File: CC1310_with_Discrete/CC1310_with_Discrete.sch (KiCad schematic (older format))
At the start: 75 parts, among them P1 CONN_02X03, P2 JTAG, P3 XBEE, SW1 RESET, SW2 USER_BUTTON, U1 TPS63051, U2 CC1310_7x7, U3 LTR-303ALS, U4 Si7006, U5 SMA_EDGE_CONNECTOR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

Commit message: added footprints the schematic
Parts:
- C1, C12, C14, C16, C17, C20, C25, C26, C28, C29, C33, C34, C8, C9, FL1: footprint (none) -> Capacitors_SMD:C_0603
- C10, C11, C13, C15, C18, C19, C2, C21, C22, C23, C24, C27, C30, C31, C32, C4, C5, C6, C7, L3, L4: footprint (none) -> Capacitors_SMD:C_0402
- C3: footprint Capacitors_SMD:C_0402 -> Capacitors_SMD:C_0603
- D1, D2, D3, D4: footprint (none) -> LEDs:LED_0805
- L1: footprint (none) -> Choke_SMD:Choke_SMD_1206_Handsoldering
- P1: footprint (none) -> Socket_Strips:Socket_Strip_Angled_2x03
- P2: footprint (none) -> Socket_Strips:Socket_Strip_Angled_2x05
- P3: footprint (none) -> Pin_Headers:Pin_Header_Straight_1x10_Pitch2.00mm
- R1, R2, R3, R4, R8, R9: footprint (none) -> Resistors_SMD:R_0402
- R10, R11, R12, R15, R7: footprint (none) -> Resistors_SMD:R_0805_HandSoldering
- R6: footprint (none) -> Resistors_SMD:R_0805
- SW1, SW2: footprint (none) -> Buttons_Switches_SMD:SW_SPST_B3U-1000P
- U1: footprint (none) -> Housings_DFN_QFN:QFN-12-1EP_3x3mm_Pitch0.5mm
- U2: footprint (none) -> Housings_DFN_QFN:QFN-48-1EP_7x7mm_Pitch0.5mm
- U3: footprint (none) -> Housings_DFN_QFN:DFN-6-1EP_2x2mm_Pitch0.65mm
- U4: footprint (none) -> Housings_DFN_QFN:DFN-6-1EP_3x3mm_Pitch0.95mm
- U6: footprint (none) -> TO_SOT_Packages_SMD:SOT-23-5
- Y1: footprint (none) -> Crystals:Crystal_FOX-FE_SMD
- Y2: value crystal -> 24 MHz; footprint (none) -> Crystals:crystal_FA238-TSX3225

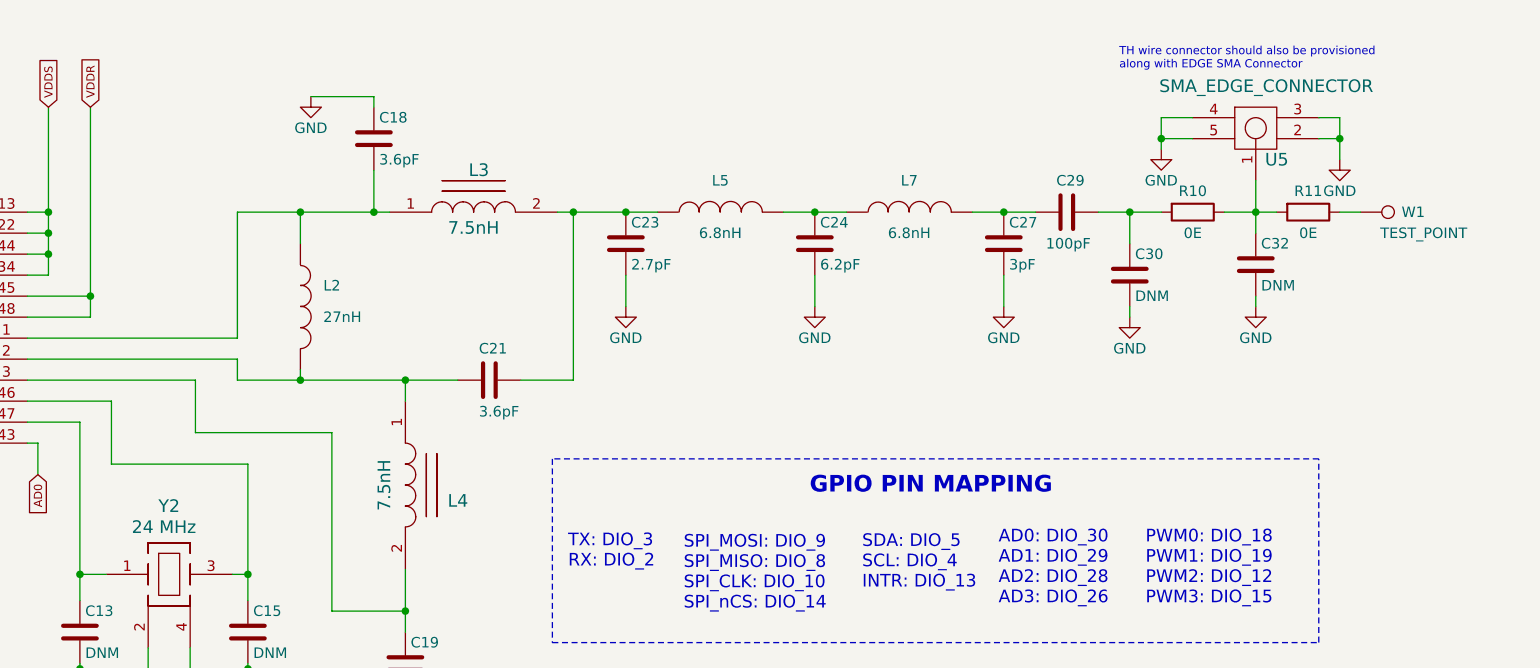
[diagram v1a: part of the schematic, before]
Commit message: verified schematic; updated library
verified both schematic
updated balun library and tps63051
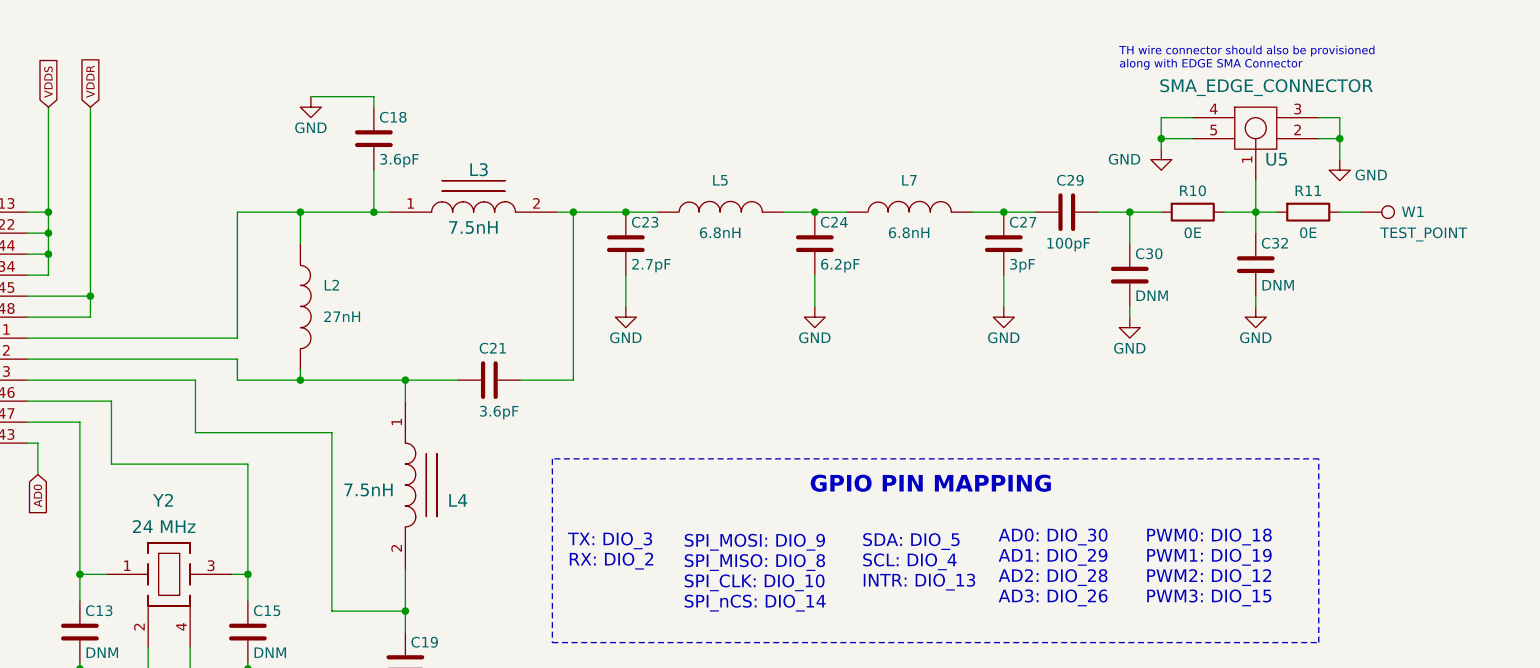
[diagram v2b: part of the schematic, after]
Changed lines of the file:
@@
 LIBS:tps63051
 LIBS:tps782
+LIBS:CC1310_with_Discrete-cache
 EELAYER 25 0
 EELAYER END
@@
 P 11450 5125
 F 0 "#PWR01" H 11450 4875 50  0001 C CNN
-F 1 "GND" H 11450 4975 50  0000 C CNN
+F 1 "GND" H 11600 5050 50  0000 C CNN
 F 2 "" H 11450 5125 50  0000 C CNN
 F 3 "" H 11450 5125 50  0000 C CNN
@@
 P 10600 5075
 F 0 "#PWR02" H 10600 4825 50  0001 C CNN
-F 1 "GND" H 10600 4925 50  0000 C CNN
+F 1 "GND" H 10425 5025 50  0000 C CNN
 F 2 "" H 10600 5075 50  0000 C CNN
 F 3 "" H 10600 5075 50  0000 C CNN
@@
 U 1 1 5832D495
 P 5775 7100
-F 0 "Y2" H 5875 7425 60  0000 C CNN
+F 0 "Y2" H 5850 7450 60  0000 C CNN
 F 1 "24 MHz" H 5850 7325 60  0000 C CNN
 F 2 "Crystals:crystal_FA238-TSX3225" H 5775 7100 60  0001 C CNN
@@
 P 7150 6475
 F 0 "L4" V 7425 6575 60  0000 C CNN
-F 1 "7.5nH" H 7350 6225 60  0000 C CNN
+F 1 "7.5nH" V 7375 6150 60  0000 C CNN
 F 2 "Capacitors_SMD:C_0402" H 7150 6475 60  0001 C CNN
 F 3 "" H 7150 6475 60  0001 C CNN
